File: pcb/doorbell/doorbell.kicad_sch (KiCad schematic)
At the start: 0 parts

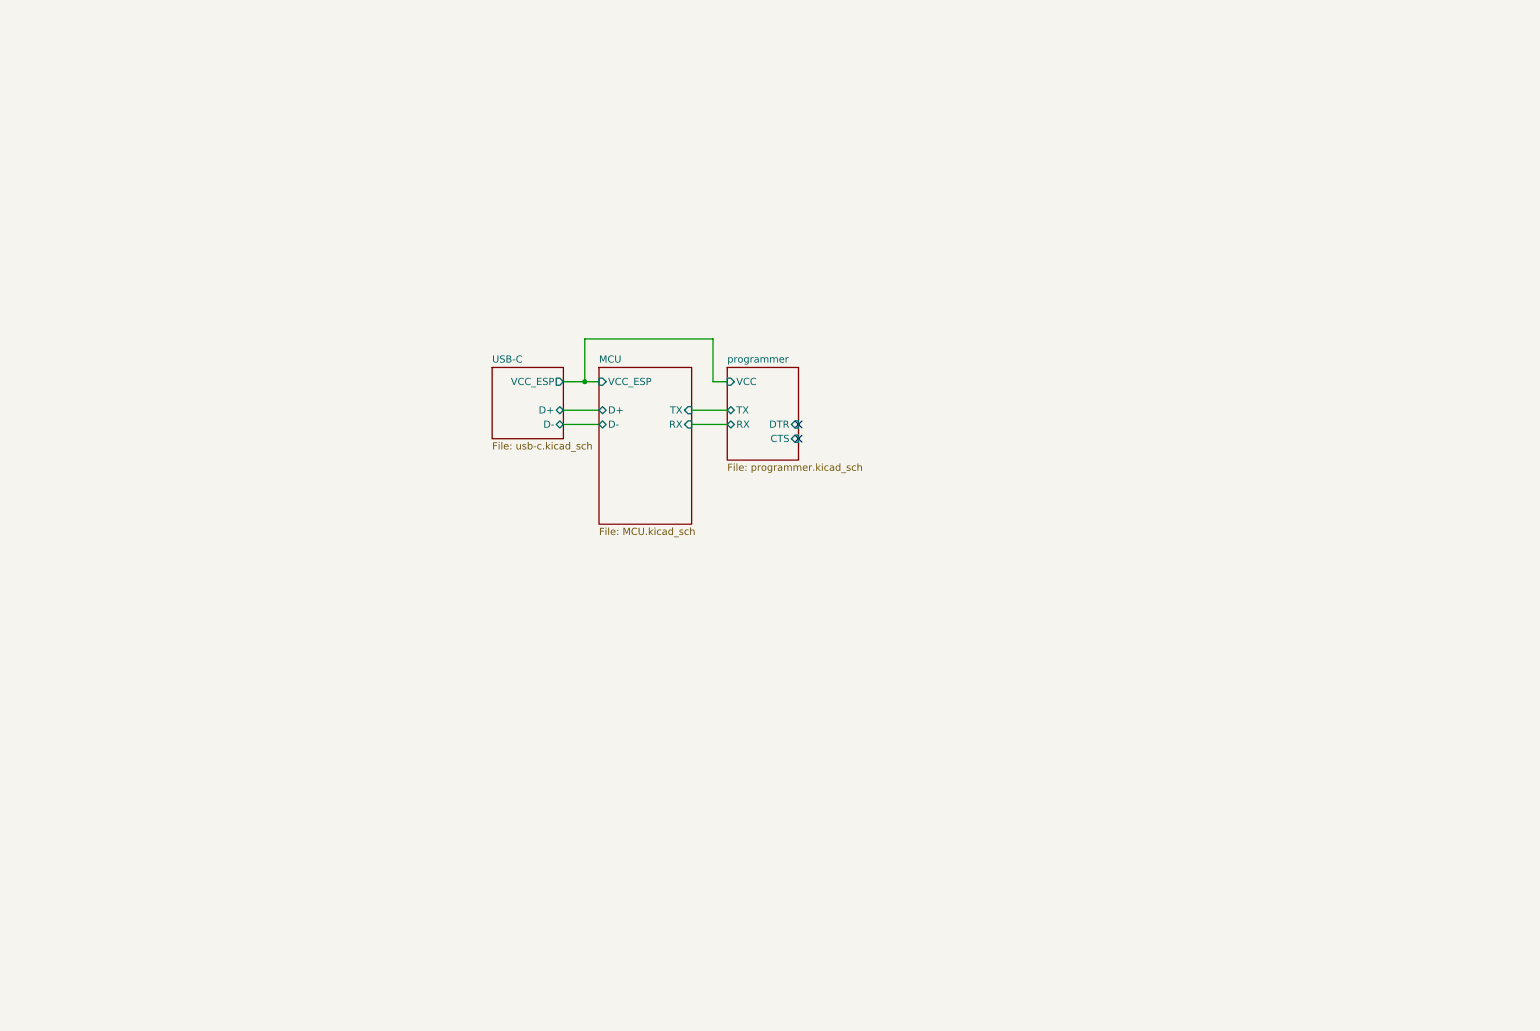
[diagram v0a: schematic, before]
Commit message: Better seperation
Added graphical seperation instead of heirarchical sheets since the
design is pretty simple. Filled out a number of missing items and
changed LDO.
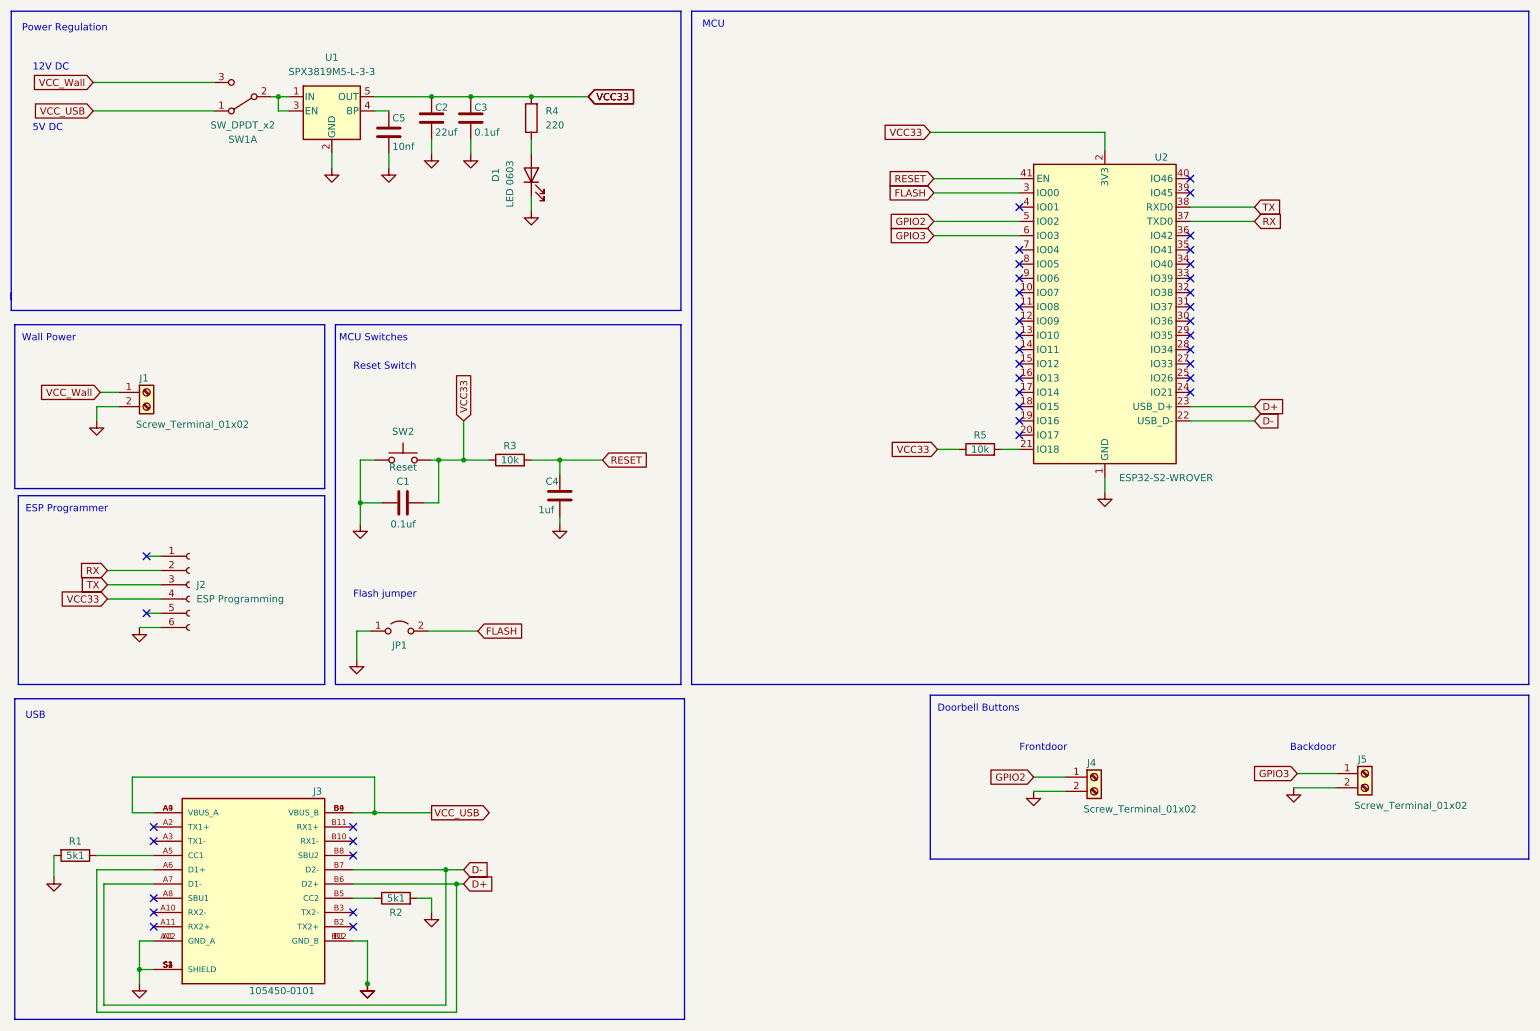
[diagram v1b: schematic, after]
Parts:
- added C1, C3: 0.1uf, symbol Device:C
- added C2: 22uf, symbol Device:C
- added C4: 1uf, symbol Device:C
- added C5: 10nf, symbol Device:C
- added D1: LED 0603, symbol Device:LED
- added J1, J4, J5: Screw_Terminal_01x02, symbol Connector:Screw_Terminal_01x02
- added J2: ESP Programming, symbol Connector:Conn_01x06_Female
- added J3: 105450-0101, MOLEX_105450-0101, symbol 105450-0101:105450-0101
- added JP1: Jumper_2_Open, symbol Jumper:Jumper_2_Open
- added R1, R2: 5k1, symbol Device:R
- added R3, R5: 10k, symbol Device:R
- added R4: 220, symbol Device:R
- added SW1: SW_DPDT_x2, symbol Switch:SW_DPDT_x2
- added SW2: Reset, symbol Switch:SW_Push
- added U1: SPX3819M5-L-3-3, Package_TO_SOT_SMD:SOT-23-5, symbol Regulator_Linear:SPX3819M5-L-3-3
- added U2: ESP32-S2-WROVER, RF_Module:ESP32-S2-WROVER, symbol RF_Module:ESP32-S2-WROVER
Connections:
- new net: C5.1, U1.4 (BP)
- new net: J3.B5 (CC2), R2.1
- new net: J3.A5 (CC1), R1.1
- new net: R5.2, U2.21 (IO18)
- new net: SW1.2 (B), U1.1 (IN), U1.3 (EN)
- new net: D1.2 (A), R4.1
- new net D+: J3.A6 (D1+), J3.B6 (D2+), U2.23 (USB_D+)
- new net D-: J3.A7 (D1-), J3.B7 (D2-), U2.22 (USB_D-)
- new net FLASH: JP1.2 (B), U2.3 (IO00)
- new net GND: C1.1, C2.2, C3.2, C4.2, C5.2, D1.1 (K), J1.2 (Pin_2), J2.6 (Pin_6), J3.A1 (GND_A), J3.A12 (GND_A), J3.B1 (GND_B), J3.B12 (GND_B), J3.S1 (SHIELD), J3.S2 (SHIELD), J3.S3 (SHIELD), J3.S4 (SHIELD), J4.2 (Pin_2), J5.2 (Pin_2), JP1.1 (A), R1.2, R2.2, SW2.1, U1.2 (GND), U2.1 (GND), U2.26 (GND), U2.42 (GND), U2.43 (GND)
- new net GPIO2: J4.1 (Pin_1), U2.5 (IO02)
- new net GPIO3: J5.1 (Pin_1), U2.6 (IO03)
- new net RESET: C4.1, R3.2, U2.41 (EN)
- new net RX: J2.2 (Pin_2), U2.37 (TXD0)
- new net TX: J2.3 (Pin_3), U2.38 (RXD0)
- new net VCC33: C1.2, C2.1, C3.1, J2.4 (Pin_4), R3.1, R4.2, R5.1, SW2.2, U1.5 (OUT), U2.2 (3V3)
- new net VCC_USB: J3.A4 (VBUS_A), J3.A9 (VBUS_A), J3.B4 (VBUS_B), J3.B9 (VBUS_B), SW1.1 (A)
- new net VCC_Wall: J1.1 (Pin_1), SW1.3 (C)
- no-connect marks 2 -> 41
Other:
- removed sheet MCU
- removed sheet USB-C
- removed sheet programmer
- note added: "12V DC"
- note added: "5V DC"
- note added: "Backdoor"
- note added: "Doorbell Buttons"
- note added: "ESP Programmer"
- note added: "Flash jumper"
- note added: "Frontdoor"
- note added: "MCU"
- note added: "MCU Switches"
- note added: "Power Regulation"
- note added: "Reset Switch"
- note added: "USB"
- note added: "Wall Power"

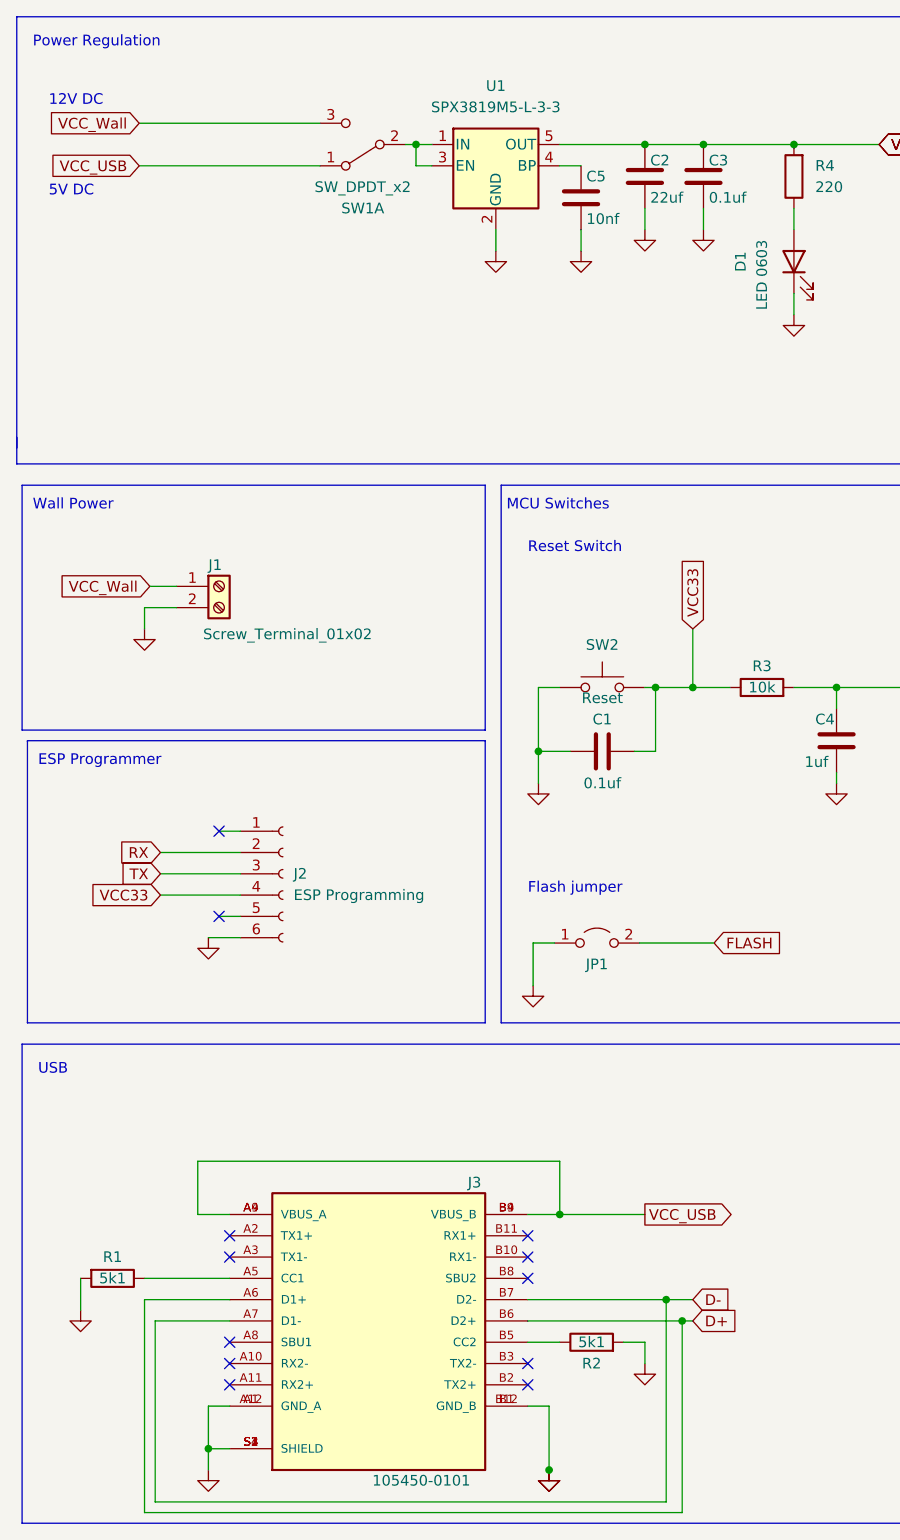
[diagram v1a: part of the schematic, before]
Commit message: v.01 done
Finished off v.01. Replaced the USB connector with a generic component
from kicad library. Also added a filter cap to the design.
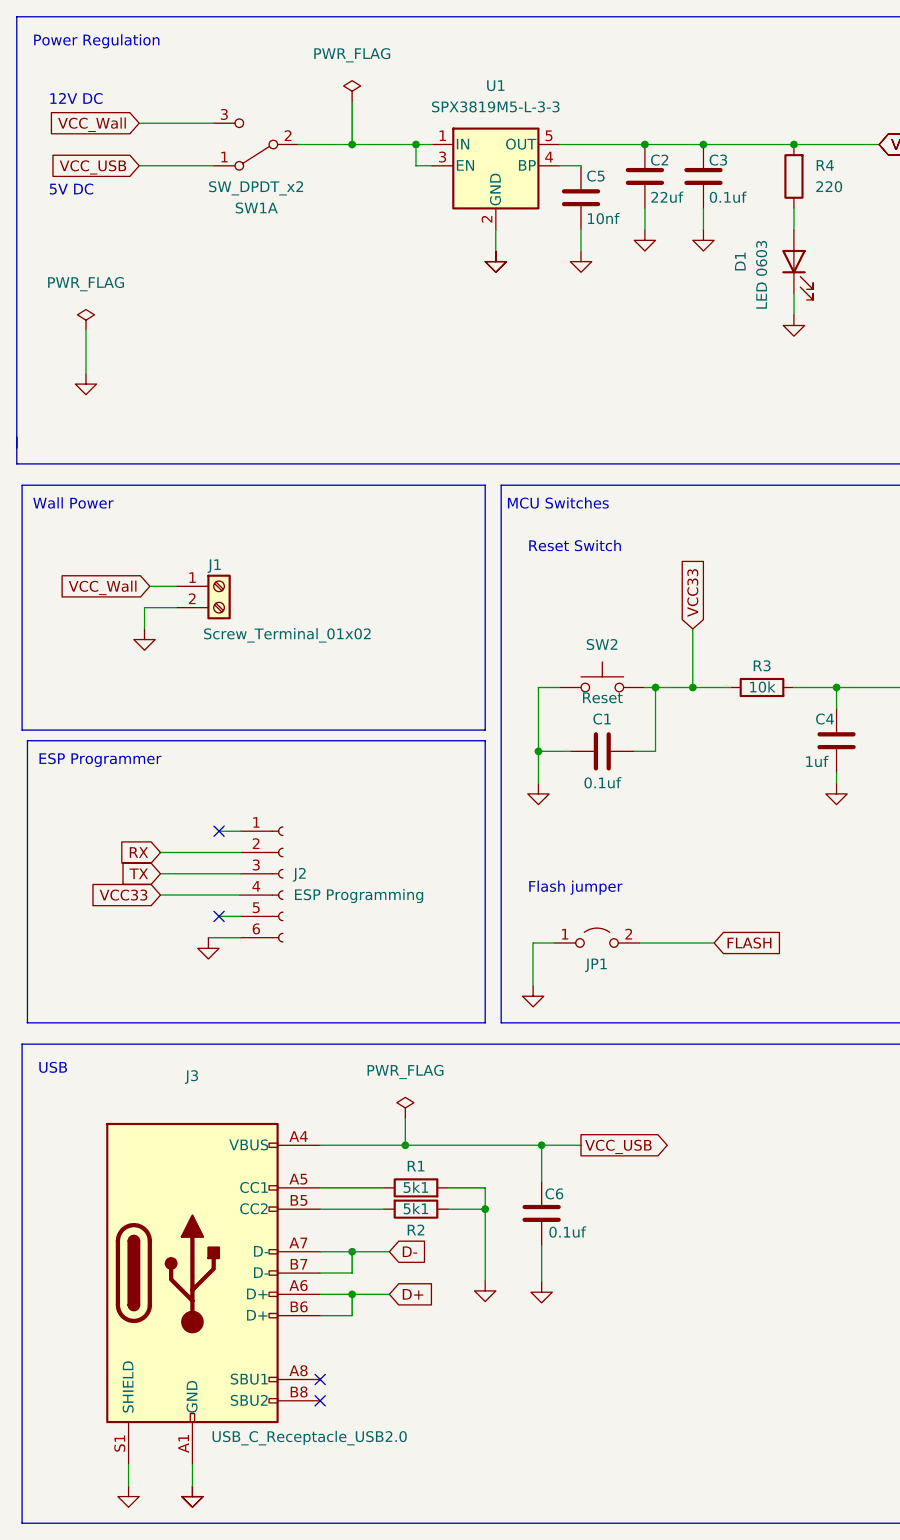
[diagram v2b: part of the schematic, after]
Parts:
- removed J3: 105450-0101, MOLEX_105450-0101, symbol 105450-0101:105450-0101
- added C6: 0.1uf, symbol Device:C
- added J3: USB_C_Receptacle_USB2.0, symbol Connector:USB_C_Receptacle_USB2.0
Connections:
- net D+: now also J3.A6 (D+), J3.B6 (D+)
- net D-: now also J3.A7 (D-), J3.B7 (D-)
- net GND: now also R2.1, C6.2, J3.A1 (GND), J3.A12 (GND), J3.B1 (GND), J3.B12 (GND), J3.S1 (SHIELD); no longer R2.2
- net VCC_USB: now also C6.1, J3.A4 (VBUS), J3.A9 (VBUS), J3.B4 (VBUS), J3.B9 (VBUS)
- net at R1.1: now also J3.A5 (CC1)
- new net: J3.B5 (CC2), R2.2
- no-connect marks 41 -> 33
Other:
- moved on the sheet: SW1A
